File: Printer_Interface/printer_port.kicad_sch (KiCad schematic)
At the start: 47 parts, among them J5 DB25_Printer, U27 74HCT574, U28 74HCT573, U29 74LVC1G06, U30 74LVC1G06, U31 74LVC1G07, U32 74LVC1G06, U33 74LVC1G14, U34 74LVC1G14, U35 74LVC1G14, U36 74LVC1G14

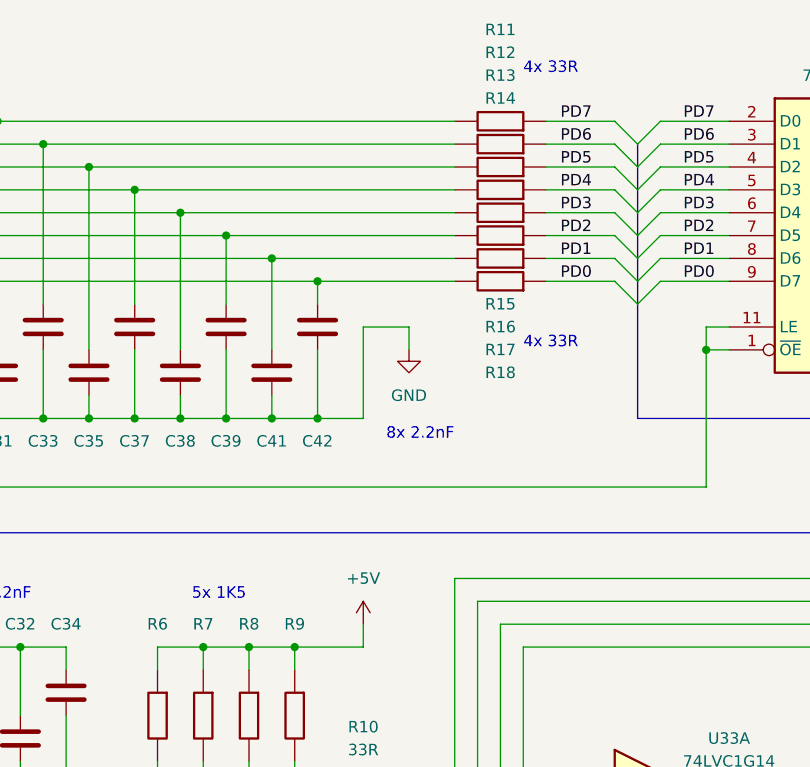
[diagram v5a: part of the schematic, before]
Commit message: Fix some typos
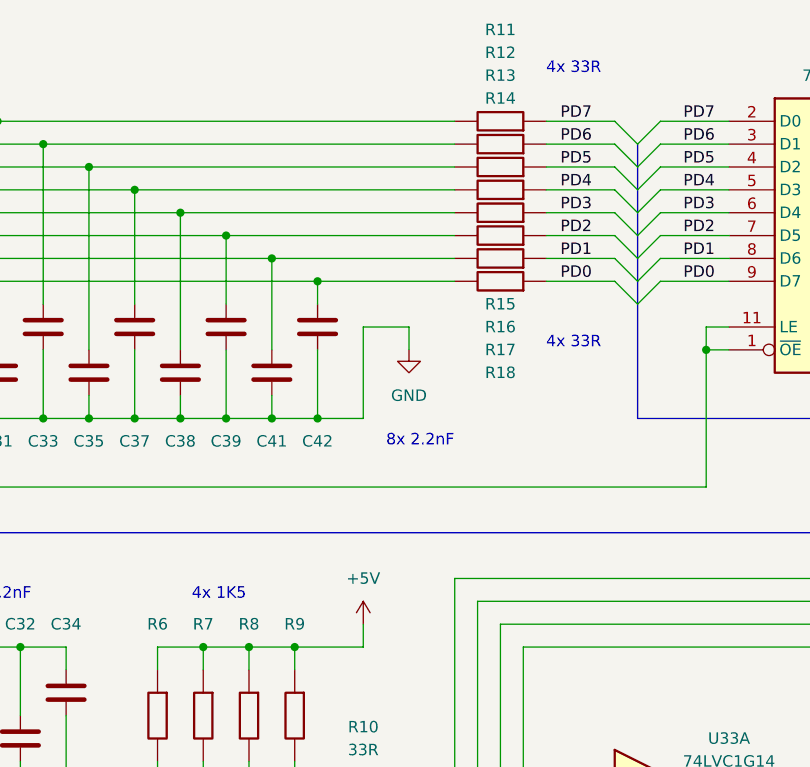
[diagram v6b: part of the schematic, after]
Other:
- note added: "4x 1K5"
- note removed: "5x 1K5"
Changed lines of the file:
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@@
 	(text "4x 33R"
 		(exclude_from_sim no)
-		(at 142.24 22.86 0)
+		(at 144.78 22.86 0)
 		(effects
 			(font
@@
 		)
 	)
-	(text "5x 1K5"
+	(text "4x 1K5"
 		(exclude_from_sim no)
 		(at 105.41 81.28 0)
@@
 	(text "4x 33R"
 		(exclude_from_sim no)
-		(at 142.24 53.34 0)
+		(at 144.78 53.34 0)
 		(effects
 			(font
@@
 				(size 1.27 1.27)
 			)
-			(justify left bottom)
+			(justify left)
 		)
 	)
